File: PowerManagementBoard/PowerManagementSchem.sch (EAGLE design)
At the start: 92 parts, among them J1 D15S24A4GV00LF, J8 182-037-213R531, J9 182-025-213R531, U1 VX7805-500, U2 PYB20-Q24-S5, U3 PYB30-Q48-S5, U4 PYB30-Q48-S12, U5 3V3REG, U6 INA4180-SPLIT, U7 INA4180-SPLIT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

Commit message: Started project for PowerTestbench
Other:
- note added: "Note: Must connect these nets!"
- note added: "What is the purpose of this header? I forget, either way it must be labelled"
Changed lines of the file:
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@@
 jig to mount to board using bolts
 and 1 wire per position.</text>
+<text x="38.1" y="175.26" size="1.778" layer="97">Note: Must connect these nets!</text>
+<text x="180.34" y="45.72" size="1.778" layer="97">What is the purpose of this header?
+I forget, either way it must be labelled</text>
 </plain>
 <instances>

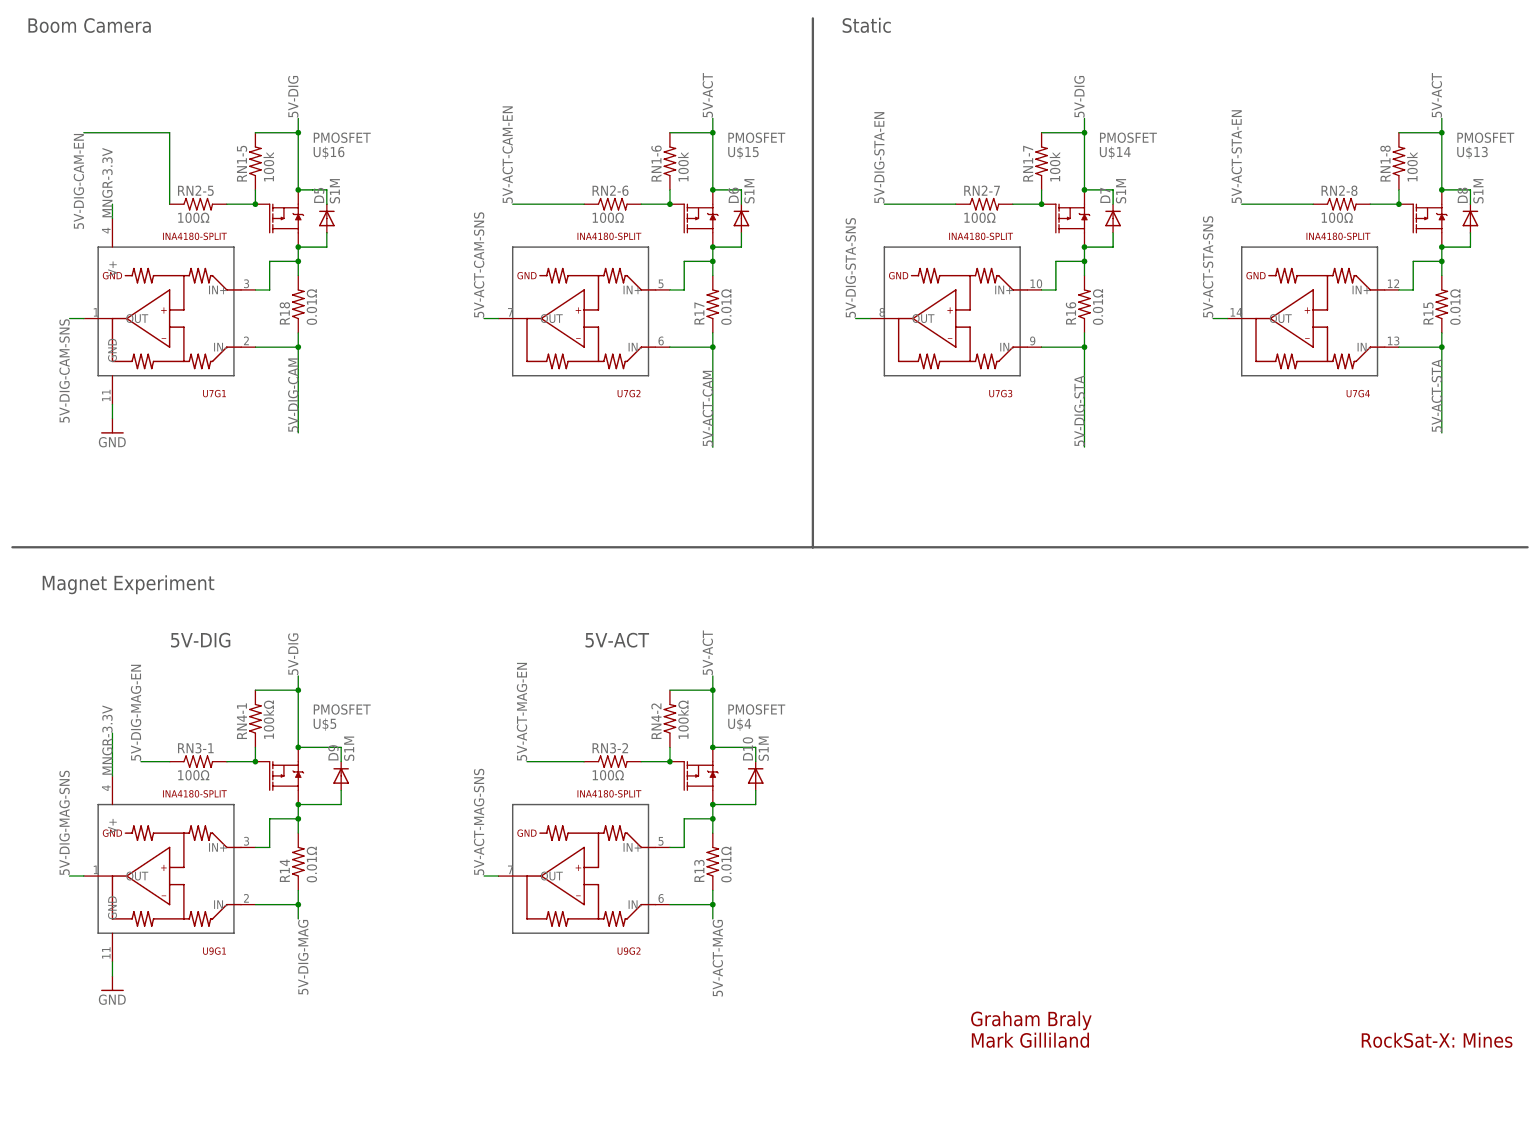
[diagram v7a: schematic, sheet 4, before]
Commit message: Replace resistor networks.
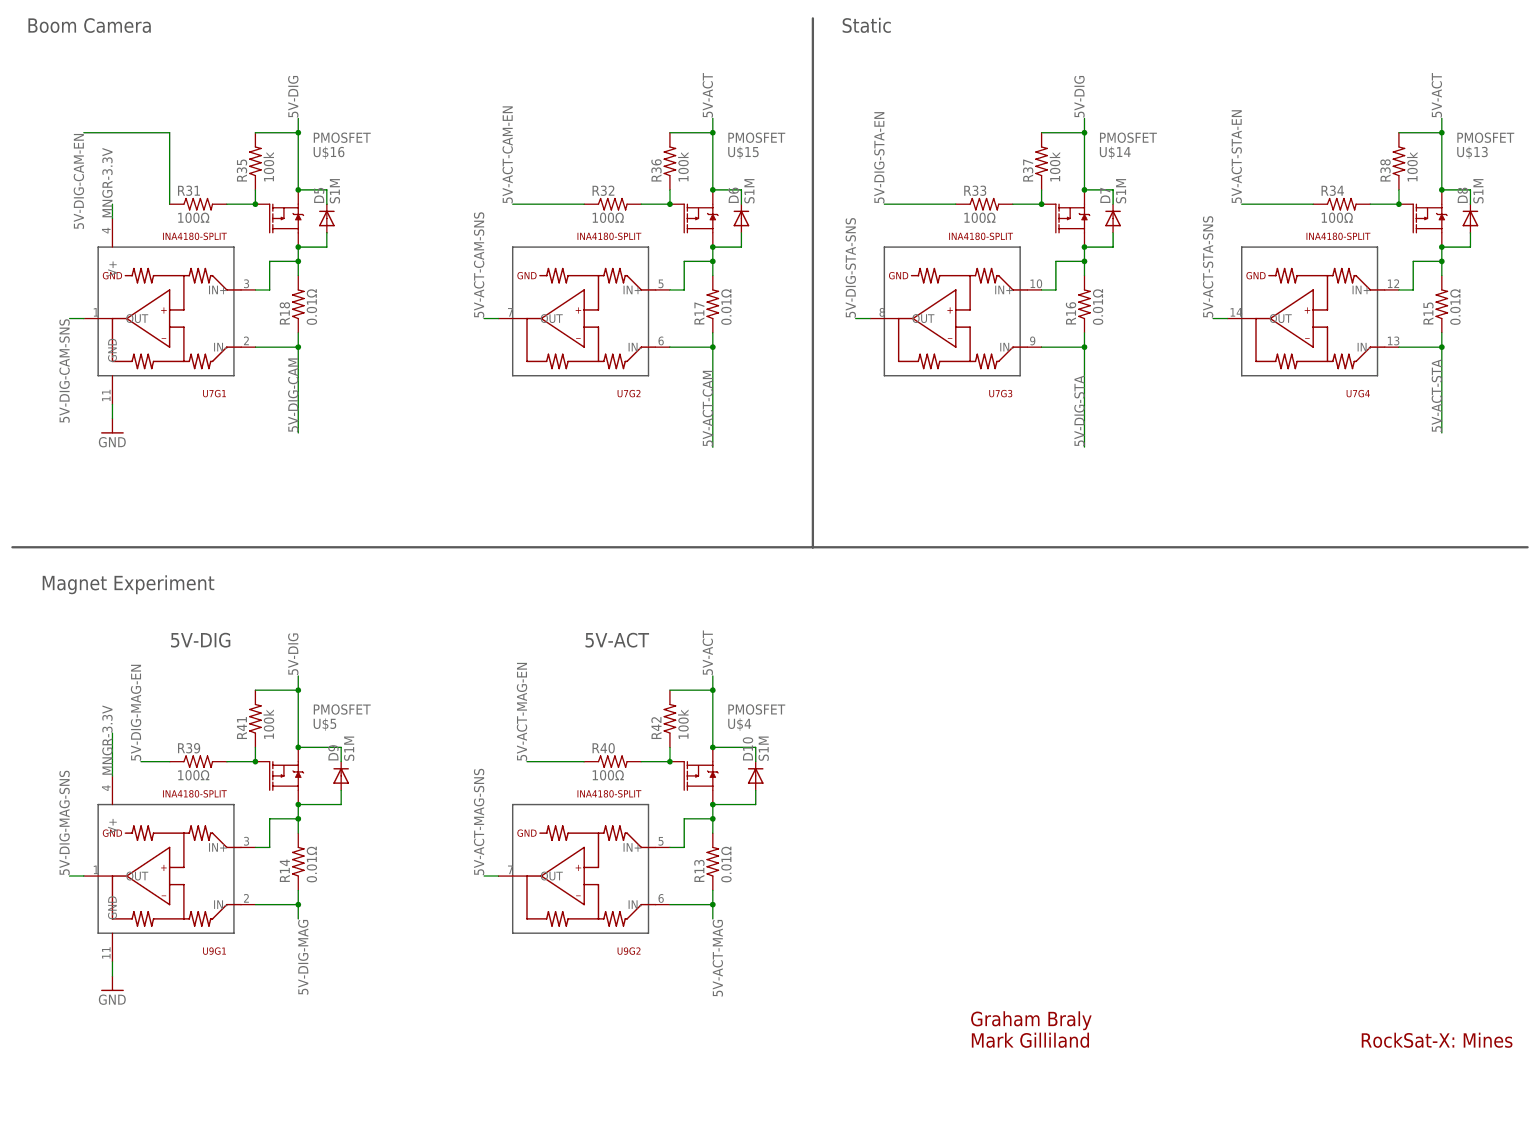
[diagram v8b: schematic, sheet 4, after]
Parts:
- removed RN1: 100k, PowerManagementParts:4816P-T01-104LF
- removed RN2, RN3: 100Ω, PowerManagementParts:4816P-T01-101LF
- removed RN4: 100kΩ, PowerManagementParts:4816P-T01-104LF
- added R23, R25, R26, R27, R35, R36, R37, R38, R41, R42, R45, R46: 100k, rcl:R-US_R0805
- added R24, R28, R29, R30, R31, R32, R33, R34, R39, R40, R43, R44: 100Ω, rcl:R-US_R0805
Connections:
- net 12V: now also R45.2, R46.2; no longer RN4-3.2, RN4-4.2
- net 12V-CAM-EN: now also R43.1; no longer RN3-3.1
- net 12V-STA-EN: now also R44.1; no longer RN3-4.1
- net 5-ACT-LASER-EN: now also R30.1; no longer RN2-4.1
- net 5V-ACT: now also R25.2, R27.2, R36.2, R38.2, R42.2; no longer RN1-2.2, RN1-4.2, RN1-6.2, RN1-8.2, RN4-2.2
- net 5V-ACT-CAM-EN: now also R32.1; no longer RN2-6.1
- net 5V-ACT-MAG-EN: now also R40.1; no longer RN3-2.1
- net 5V-ACT-STA-EN: now also R34.1; no longer RN2-8.1
- net 5V-ACT-TX-EN: now also R28.1; no longer RN2-2.1
- net 5V-DIG: now also R23.2, R26.2, R35.2, R37.2, R41.2; no longer RN1-1.2, RN1-3.2, RN1-5.2, RN1-7.2, RN4-1.2
- net 5V-DIG-CAM-EN: now also R31.1; no longer RN2-5.1
- net 5V-DIG-LASER-EN: now also R29.1; no longer RN2-3.1
- net 5V-DIG-MAG-EN: now also R39.1; no longer RN3-1.1
- net 5V-DIG-STA-EN: now also R33.1; no longer RN2-7.1
- net 5V-DIG-TX-EN: now also R24.1; no longer RN2-1.1
- net N$10: now also R25.1, R28.2; no longer RN1-2.1, RN2-2.2
- net N$13: now also R26.1, R29.2; no longer RN1-3.1, RN2-3.2
- net N$15: now also R27.1, R30.2; no longer RN1-4.1, RN2-4.2
- net N$21: now also R40.2, R42.1; no longer RN3-2.2, RN4-2.1
- net N$23: now also R39.2, R41.1; no longer RN3-1.2, RN4-1.1
- net N$25: now also R34.2, R38.1; no longer RN1-8.1, RN2-8.2
- net N$27: now also R33.2, R37.1; no longer RN1-7.1, RN2-7.2
- net N$29: now also R32.2, R36.1; no longer RN1-6.1, RN2-6.2
- net N$31: now also R31.2, R35.1; no longer RN1-5.1, RN2-5.2
- net N$40: now also R43.2, R45.1; no longer RN3-3.2, RN4-3.1
- net N$43: now also R44.2, R46.1; no longer RN3-4.2, RN4-4.1
- net N$9: now also R23.1, R24.2; no longer RN1-1.1, RN2-1.2
